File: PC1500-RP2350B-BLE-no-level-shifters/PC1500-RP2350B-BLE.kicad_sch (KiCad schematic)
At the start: 44 parts, among them J1 microSD, J2 USB-C (programming/debug), J3 PC-1500 40-pin cartridge slot, J5 PC1500_SENSE_JUMPER, J6 SPARE_GPIO_U9, J7 SWD_I2C_HEADER, SW1 BOOTSEL, U1 RP2350B, U10 TCA9406DCUR, U11 FXMA108, U12 FXMA108, U2 AS6C62256-55STCN, U3 SLG46826V, U4 AP2112K-3.3, U5 W25Q32RVXHJQ, U7 FXMA108, U8 RN4871, U9 SLG46826V, X1 12MHz (Abracon ABM8-272-T3)

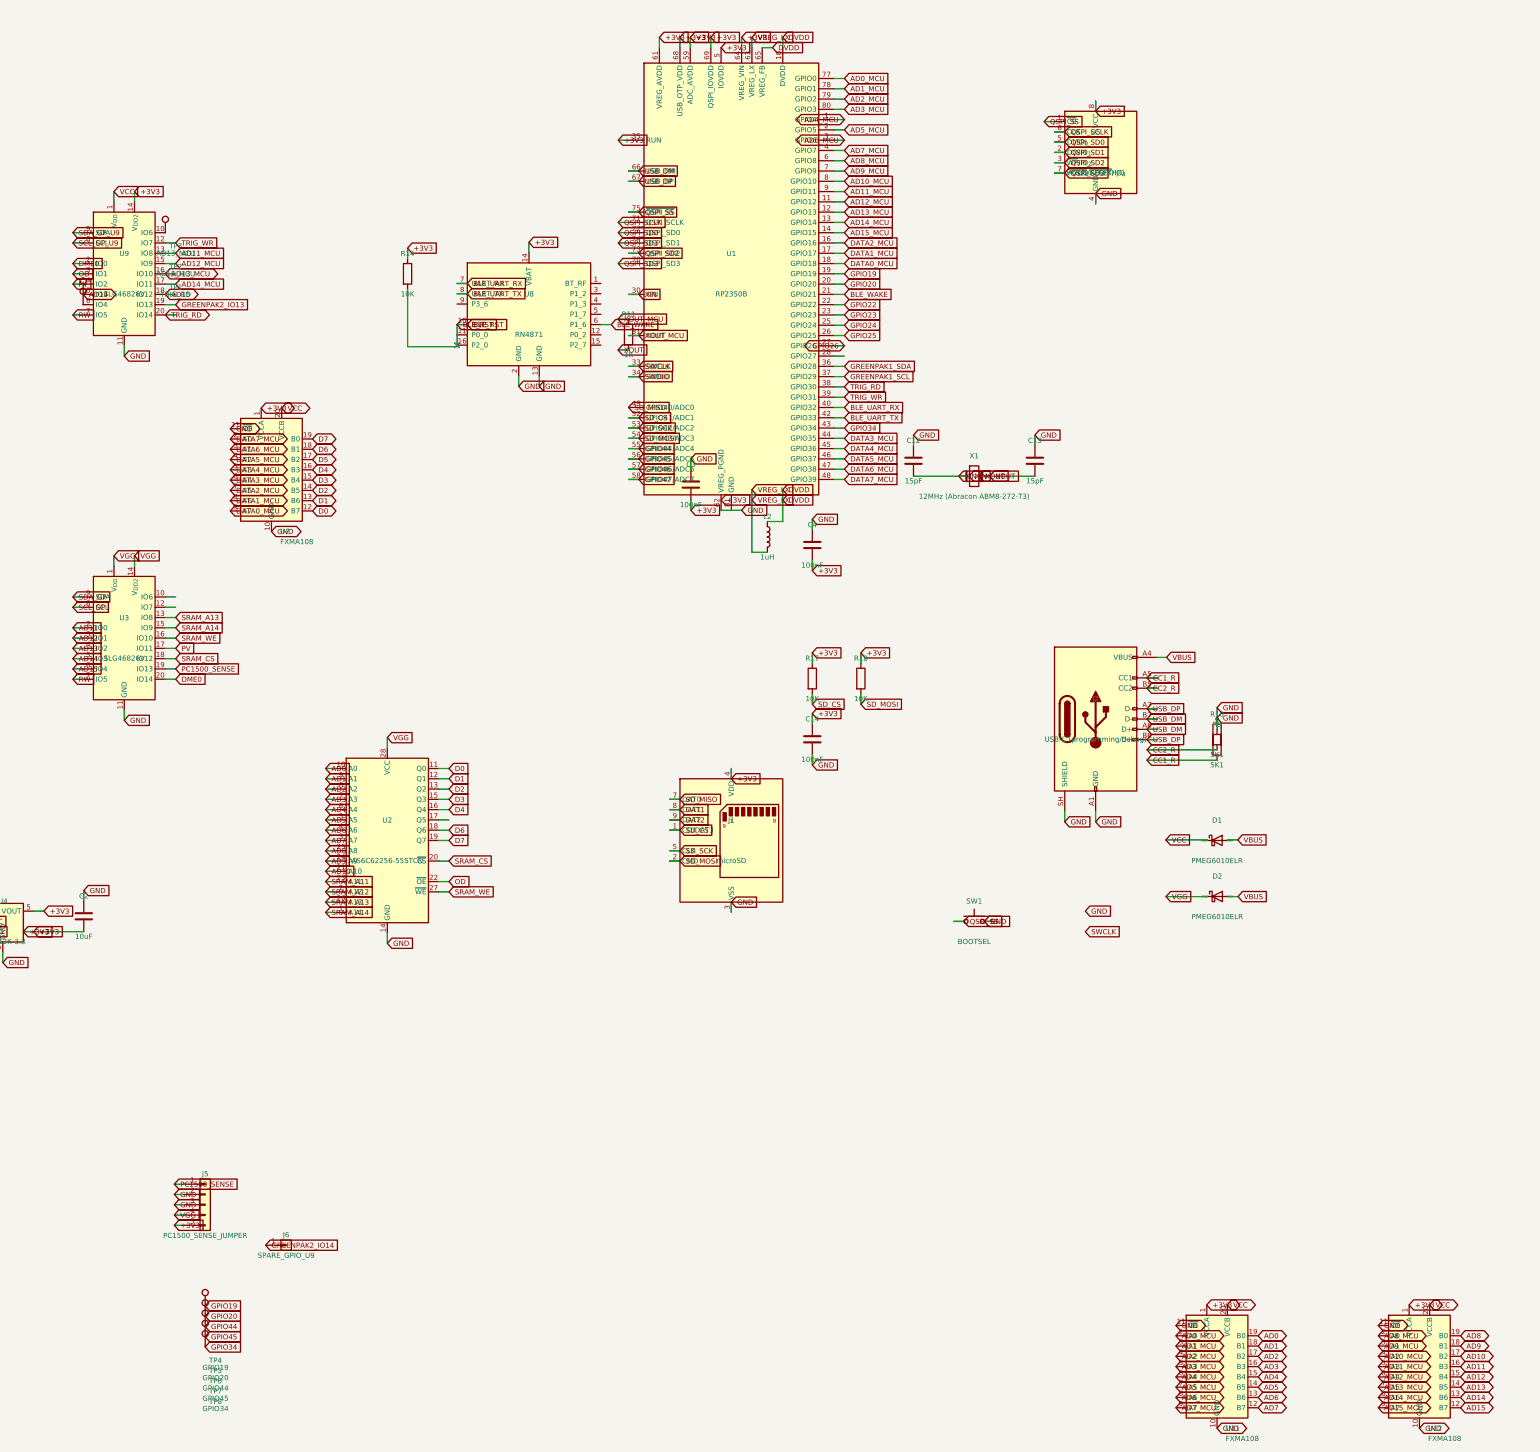
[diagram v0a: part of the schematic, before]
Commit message: Add GreenPak bench-test/provisioning tools and no-level-shifters board variants
- GreenPakTester: standalone Pico 2 W bench-test firmware for the
  GreenPAK SLG46826V, with a VS-Code-extension-friendly project layout
  (Run/Flash/Serial-Monitor buttons via the Raspberry Pi Pico extension).
- GreenPak_Provision: standalone GreenPAK NVM provisioner, split out of
  RP2350's multi-target CMakeLists.txt into its own extension-friendly
  project for the same easy build/flash/serial-monitor workflow.
- PC1500-Pico2W-Dongle and PC1500-RP2350B-BLE: latest schematic/PCB
  edits, plus a new no-level-shifters KiCad variant of each board.
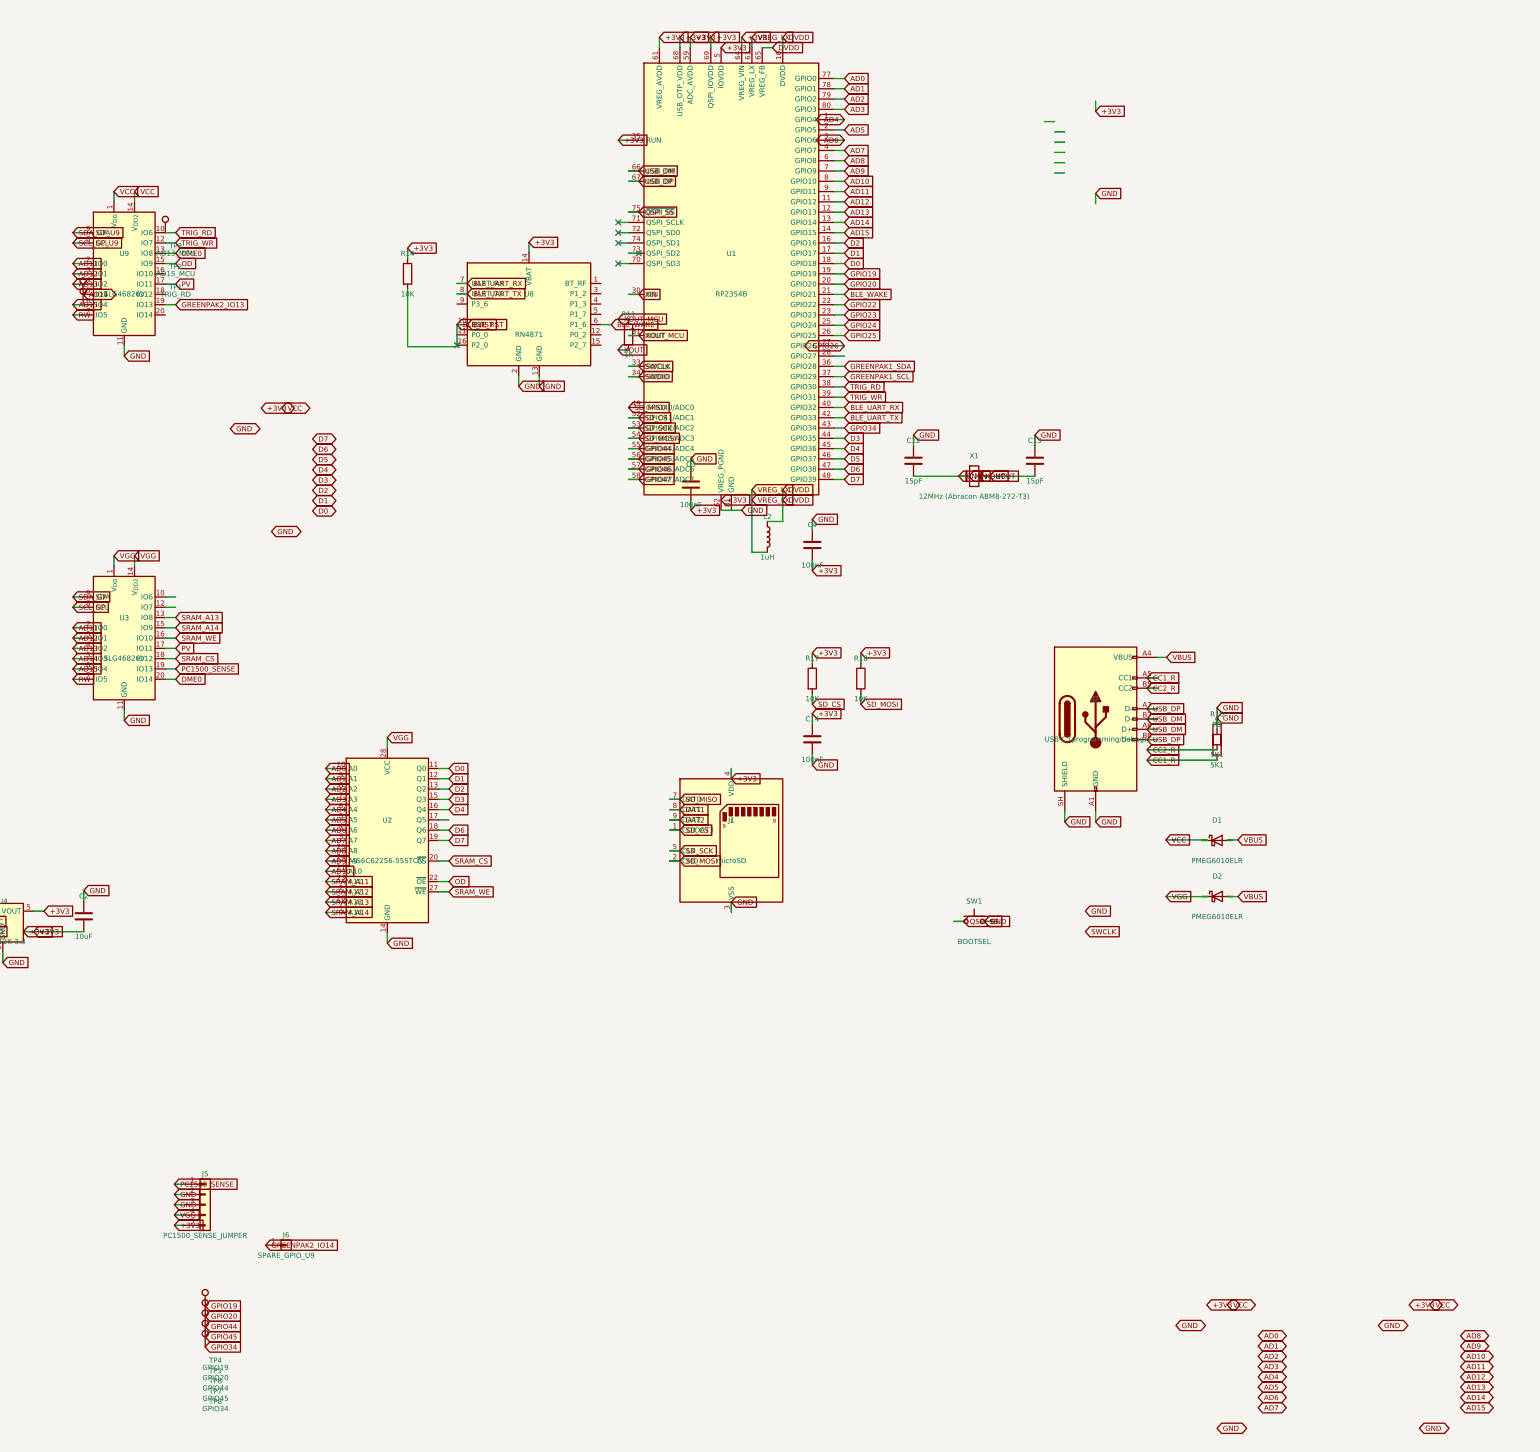
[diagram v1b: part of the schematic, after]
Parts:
- removed U11, U12, U7: FXMA108, Package_DFN_QFN:WQFN-20-1EP_2.5x4.5mm_P0.5mm_EP1x2.9mm, symbol Logic_LevelTranslator:FXMA108
- removed U5: W25Q32RVXHJQ, Package_SO:SOIC-8_3.9x4.9mm_P1.27mm, symbol Memory_Flash:W25Q32JVSS
- U1: value RP2350B -> RP2354B; symbol MCU_RaspberryPi:RP2350B -> MCU_RaspberryPi:RP2354B
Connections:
- net AD0_MCU is gone; now on net AD0: U1.77 (GPIO0)
- net AD10_MCU is gone; now on net AD10: U1.8 (GPIO10)
- net AD15_MCU is gone; now on net AD15: U1.14 (GPIO15)
- net AD1_MCU is gone; now on net AD1: U1.78 (GPIO1)
- net AD2_MCU is gone; now on net AD2: U1.79 (GPIO2)
- net AD3_MCU is gone; now on net AD3: U1.80 (GPIO3)
- net AD4_MCU is gone; now on net AD4: U1.1 (GPIO4)
- net AD5_MCU is gone; now on net AD5: U1.2 (GPIO5)
- net AD6_MCU is gone; now on net AD6: U1.3 (GPIO6)
- net AD7_MCU is gone; now on net AD7: U1.4 (GPIO7)
- net AD8_MCU is gone; now on net AD8: U1.6 (GPIO8)
- net AD9_MCU is gone; now on net AD9: U1.7 (GPIO9)
- net DATA0_MCU is gone; now on net D0: U1.18 (GPIO18)
- net DATA1_MCU is gone; now on net D1: U1.17 (GPIO17)
- net DATA2_MCU is gone; now on net D2: U1.16 (GPIO16)
- net DATA3_MCU is gone; now on net D3: U1.44 (GPIO35)
- net DATA4_MCU is gone; now on net D4: U1.45 (GPIO36)
- net DATA5_MCU is gone; now on net D5: U1.46 (GPIO37)
- net DATA6_MCU is gone; now on net D6: U1.47 (GPIO38)
- net DATA7_MCU is gone; now on net D7: U1.48 (GPIO39)
- net +3V3: no longer U9.14 (V_{DD2})
- net AD11: now also U1.9 (GPIO11), U9.2 (IO0)
- net AD12: now also U1.11 (GPIO12), U9.3 (IO1)
- net AD13: now also U1.12 (GPIO13), U9.4 (IO2)
- net AD14: now also U1.13 (GPIO14)
- net AD15: now also TP3.1, U9.6 (IO4); no longer U9.18 (IO12)
- net DME0: now also U9.13 (IO8); no longer U9.2 (IO0)
- net OD: now also U9.15 (IO9); no longer U9.3 (IO1)
- net PV: now also U9.17 (IO11); no longer U9.4 (IO2)
- net TRIG_RD: now also TP1.1, U9.10 (IO6); no longer U9.20 (IO14)
- net VCC: now also U9.14 (V_{DD2})
- removed net AD11_MCU: U1.9 (GPIO11), U9.13 (IO8)
- removed net AD12_MCU: U1.11 (GPIO12), U9.15 (IO9)
- net AD13_MCU: no longer names the net of U9.16 (IO10)
- net AD13_MCU: no longer U1.12 (GPIO13)
- removed net AD14_MCU: U1.13 (GPIO14), U9.17 (IO11)
- net QSPI_SCLK: no longer names the net of U1.71 (QSPI_SCLK)
- net QSPI_SD0: no longer names the net of U1.72 (QSPI_SD0)
- net QSPI_SD1: no longer names the net of U1.74 (QSPI_SD1)
- net QSPI_SD2: no longer names the net of U1.73 (QSPI_SD2)
- net QSPI_SD3: no longer names the net of U1.70 (QSPI_SD3)
- no-connect marks 1 -> 6
